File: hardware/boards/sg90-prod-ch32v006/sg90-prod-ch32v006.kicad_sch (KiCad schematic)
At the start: 36 parts, among them J1 Servo Input, J2 Motor, J3 Debug, J4 Potentiometer, Q1 AO3401A, U1 TPAP2210K-3.3TRG1, U2 SN74LVC2G07DRYR(UMW), U3 DRV8837DSGR-JSM, U4 CH32V006F8U6

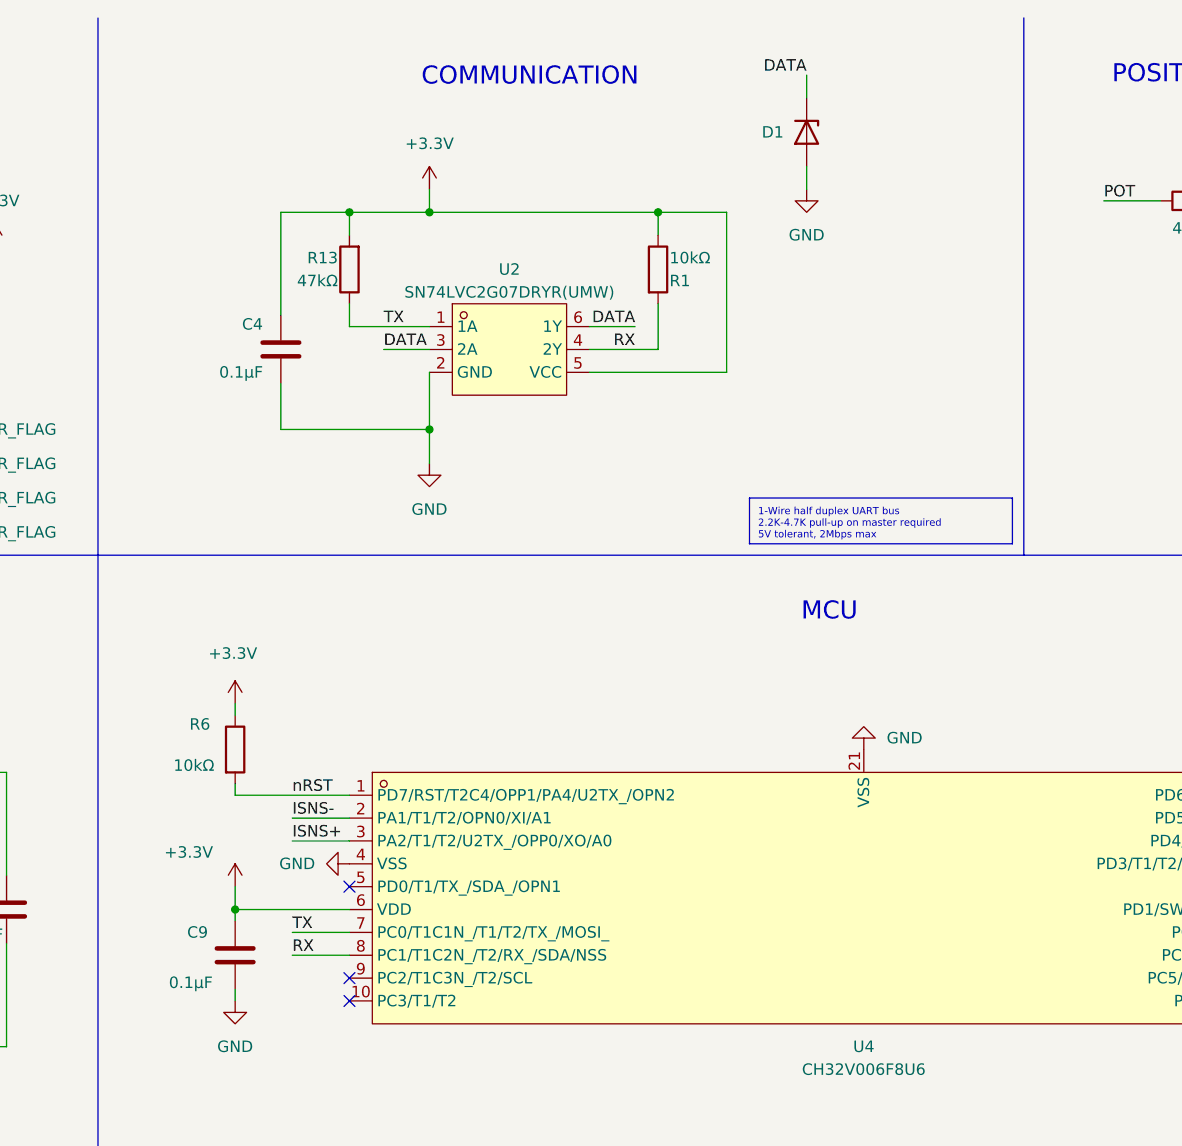
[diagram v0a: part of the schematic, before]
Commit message: Add X2-DFN1210-8 footprint and update schematics
- Add X2-DFN1210-8 footprint (1.2x1.0mm, 8-pin DFN)
- Add 3D models (STEP and WRL)
- Update shared symbol library
- Update sg90-prod-ch32v006 schematic
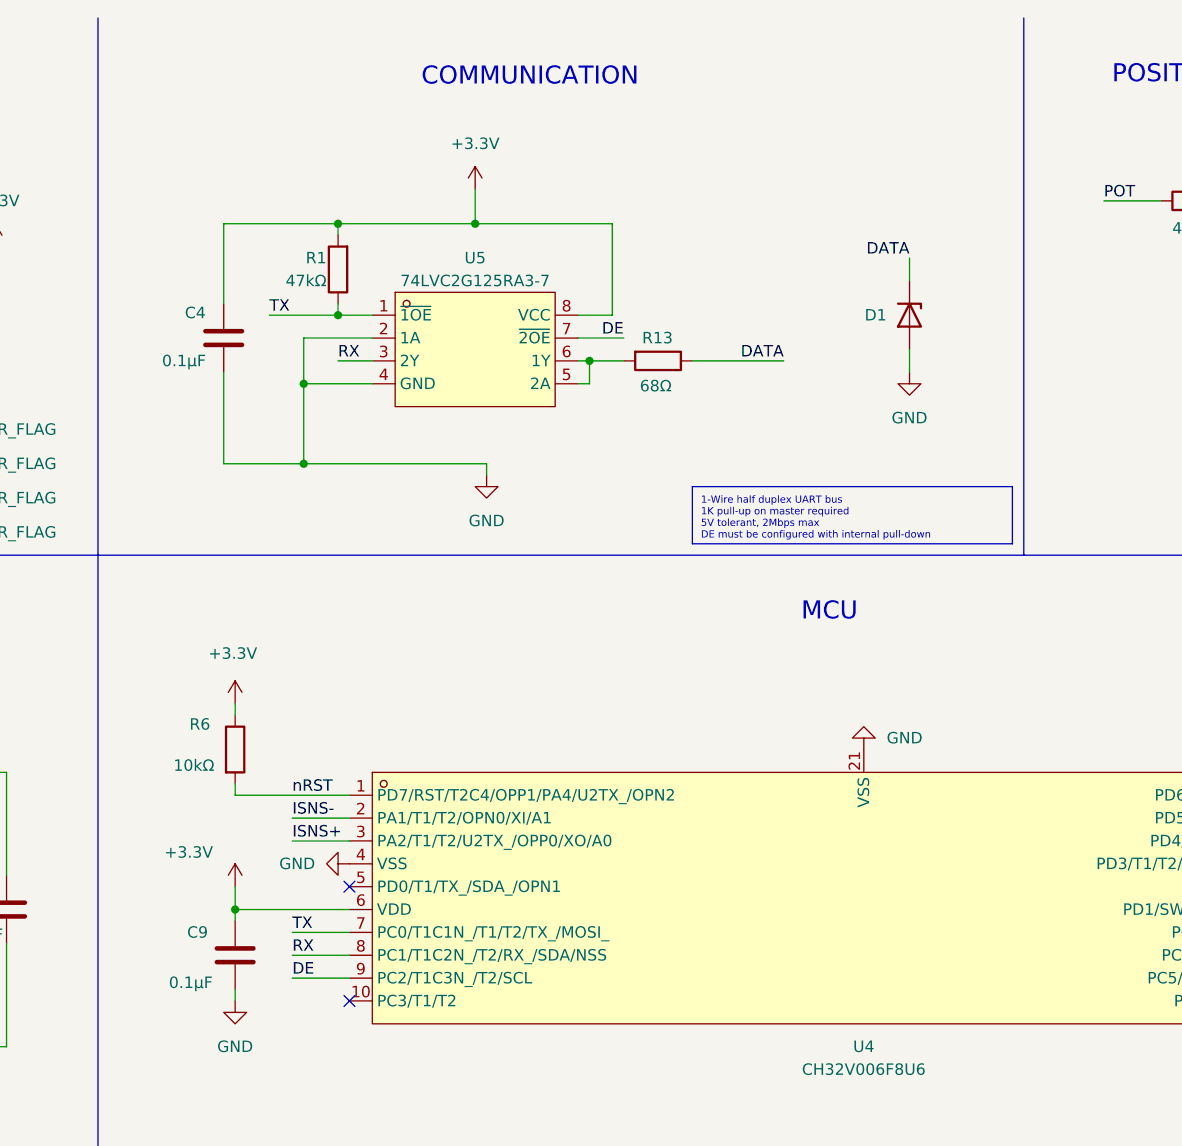
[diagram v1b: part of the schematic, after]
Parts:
- removed U2: SN74LVC2G07DRYR(UMW), shared:SON-6_L1.5-W1.0-P0.50-BL, symbol shared:SN74LVC2G07DRYR(UMW)
- added U5: 74LVC2G125RA3-7, shared:X2-DFN1210-8_L1.2-W1.0-P0.30-BL, symbol shared:74LVC2G125RA3-7
- R1: value 10kΩ -> 47kΩ; LCSC C11702 -> C25792
- R13: value 47kΩ -> 68Ω
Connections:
- net +3.3V: now also R1.2, U5.8 (VCC); no longer R1.1, R13.2
- net DATA: now also R13.1
- net GND: now also U5.2 (1A), U5.4 (GND)
- net RX: now also U5.3 (2Y); no longer R1.2
- net TX: now also R1.1, U5.1 (~{1OE}); no longer R13.1
- net DE: now reaches U4.9 (PC2/T1C3N_/T2/SCL)
- net DE: now also U5.7 (~{2OE})
- new net: R13.2, U5.5 (2A), U5.6 (1Y)
- no-connect marks 3 -> 2
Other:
- moved on the sheet: C4, D1

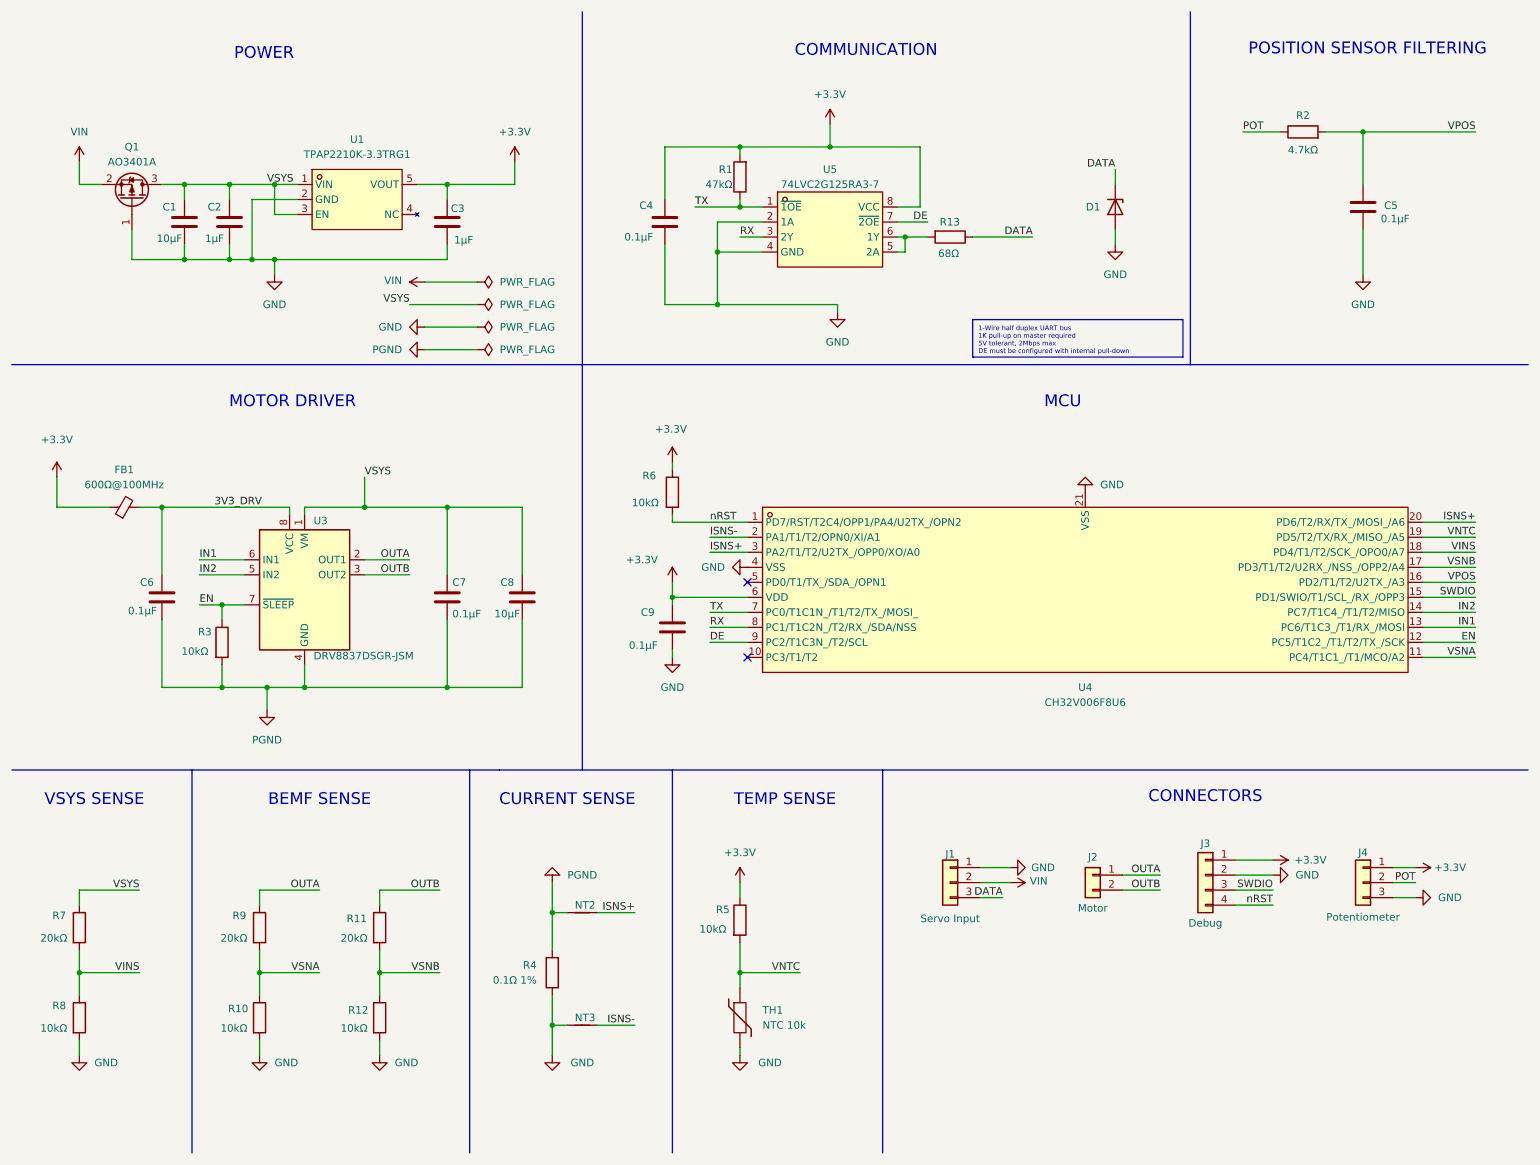
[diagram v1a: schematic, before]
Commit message: echo-free data line with RX disable latch
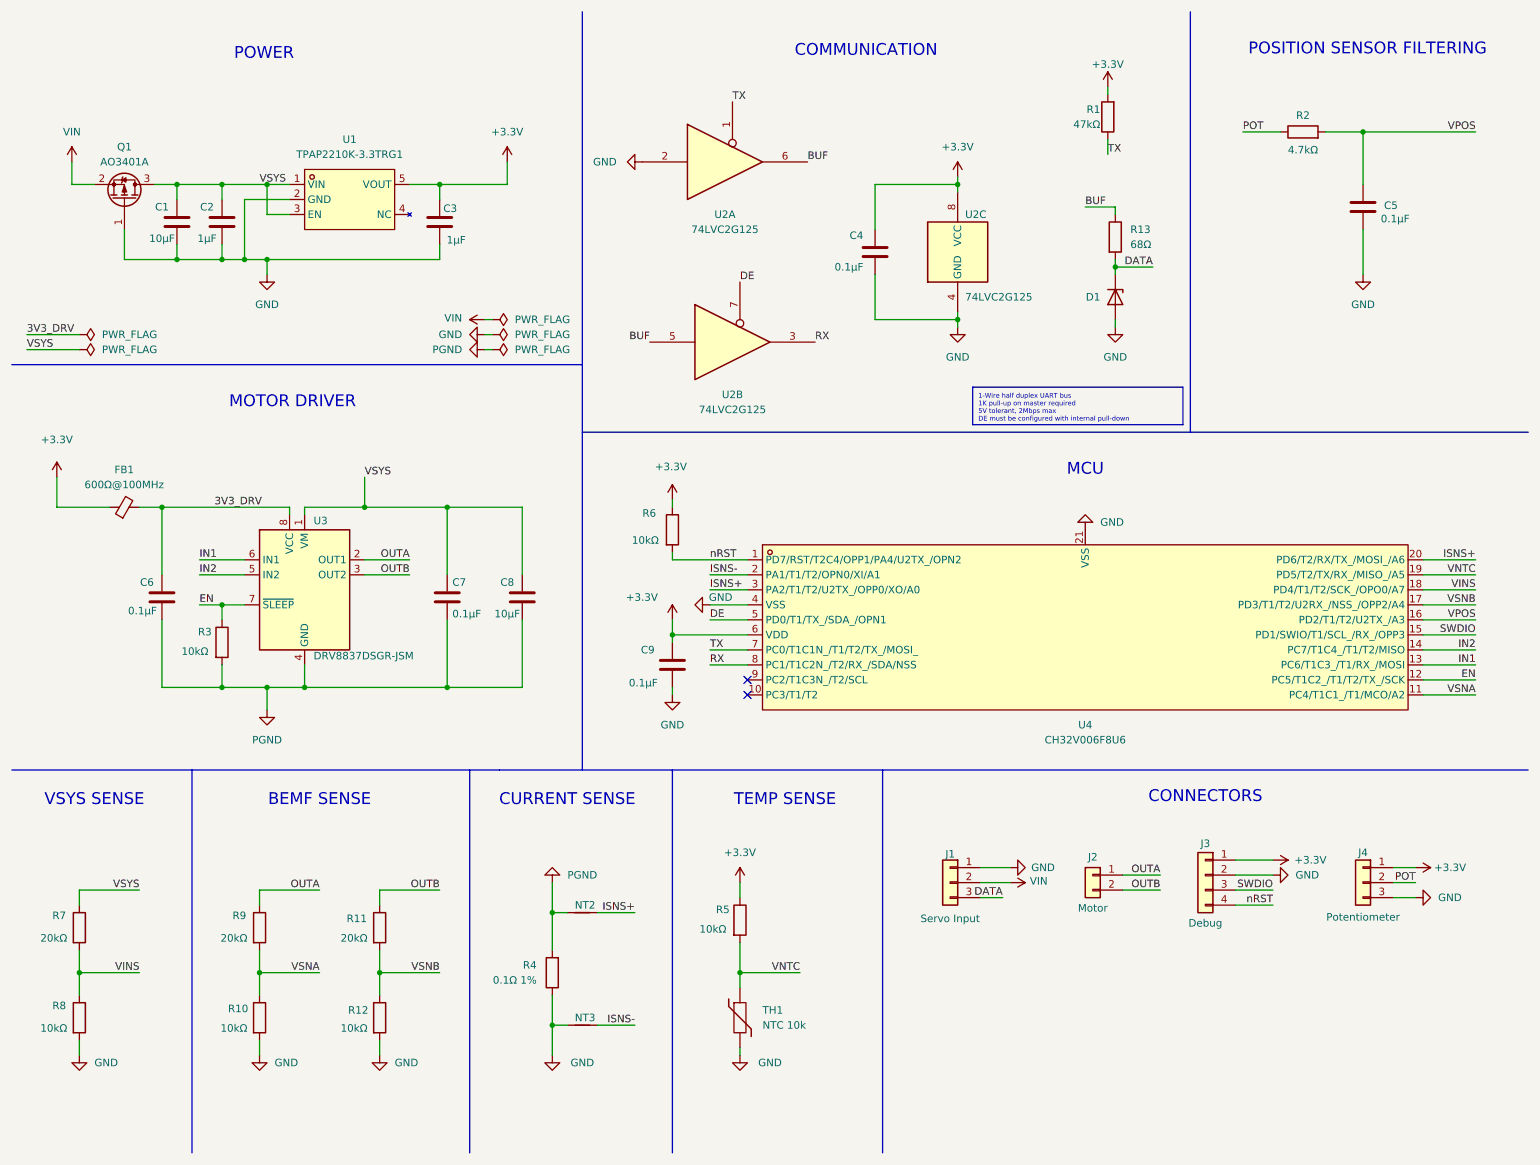
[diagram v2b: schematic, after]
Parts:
- removed U5: 74LVC2G125RA3-7, shared:X2-DFN1210-8_L1.2-W1.0-P0.30-BL, symbol shared:74LVC2G125RA3-7
- added U2: 74LVC2G125, shared:X2-DFN1210-8_L1.2-W1.0-P0.30-BL, symbol 74xGxx:74LVC2G125
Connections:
- net +3.3V: now also U2.8 (VCC)
- net DATA: now also R13.2; no longer R13.1
- net DE: now also U4.5 (PD0/T1/TX_/SDA_/OPN1), U2.7; no longer U4.9 (PC2/T1C3N_/T2/SCL)
- net GND: now also U2.2, U2.4 (GND)
- net RX: now also U2.3
- net TX: now also U2.1
- new net BUF: R13.1, U2.5, U2.6
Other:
- moved on the sheet: C1, C2, C3, C9, D1, Q1, R13, R6, U1, U4

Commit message: Normalize line endings to LF
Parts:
- removed NT3: NetTie_2, shared:NetTie-2_SMD_0.2mm, symbol Device:NetTie_2
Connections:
- net ISNS+ renamed ISNS
- net ISNS-: no longer names the net of U4.2 (PA1/T1/T2/OPN0/XI/A1)
- no-connect marks 2 -> 3
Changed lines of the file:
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@@
 	)
 	(junction
-		(at 102.87 182.88)
-		(diameter 0)
-		(color 0 0 0 0)
-	)
-	(junction
 		(at 73.66 173.99)
 		(diameter 0)
@@
 		(at 135.89 127)
 	)
+	(no_connect
+		(at 135.89 106.68)
+	)
 	(wire
 		(pts
@@
 	(wire
 		(pts
-			(xy 116.84 182.88) (xy 110.49 182.88)
-		)
-		(stroke
-			(width 0)
-			(type default)
-		)
-	)
-	(wire
-		(pts
 			(xy 91.44 63.5) (xy 92.71 63.5)
 		)
@@
 	(wire
 		(pts
-			(xy 102.87 182.88) (xy 102.87 187.96)
+			(xy 102.87 177.8) (xy 102.87 187.96)
 		)
 		(stroke
@@
 	(wire
 		(pts
-			(xy 105.41 182.88) (xy 102.87 182.88)
-		)
-		(stroke
-			(width 0)
-			(type default)
-		)
-	)
-	(wire
-		(pts
 			(xy 30.48 48.26) (xy 30.48 53.34)
 		)
@@
 	(wire
 		(pts
-			(xy 129.54 106.68) (xy 135.89 106.68)
-		)
-		(stroke
-			(width 0)
-			(type default)
-		)
-	)
-	(wire
-		(pts
 			(xy 196.85 24.13) (xy 196.85 25.4)
 		)
@@
 	(wire
 		(pts
-			(xy 102.87 177.8) (xy 102.87 182.88)
-		)
-		(stroke
-			(width 0)
-			(type default)
-		)
-	)
-	(wire
-		(pts
 			(xy 180.34 156.21) (xy 175.26 156.21)
 		)
@@
 		)
 	)
-	(label "ISNS+"
+	(label "ISNS"
 		(at 259.08 104.14 180)
 		(effects
@@
 		)
 	)
-	(label "ISNS-"
-		(at 129.54 106.68 0)
-		(effects
-			(font
-				(size 1.27 1.27)
-			)
-			(justify left bottom)
-		)
-	)
 	(label "TX"
 		(at 196.85 35.56 0)
@@
 		)
 	)
-	(label "ISNS+"
+	(label "ISNS"
 		(at 129.54 109.22 0)
 		(effects
@@
 		)
 	)
-	(label "ISNS+"
+	(label "ISNS"
 		(at 116.84 163.83 180)
 		(effects
@@
 		)
 	)
-	(label "ISNS-"
-		(at 116.84 182.88 180)
-		(effects
-			(font
-				(size 1.27 1.27)
-			)
-			(justify right bottom)
-		)
-	)
 	(label "DATA"
 		(at 204.47 54.61 180)
@@
 					(unit 1)
 				)
-			)
-		)
-	)
-	(symbol
-		(lib_id "Device:NetTie_2")
-		(at 107.95 182.88 180)
-		(unit 1)
-		(exclude_from_sim no)
-		(in_bom no)
-		(on_board yes)
-		(dnp no)
-		(property "Reference" "NT3"
-			(at 106.68 181.61 0)
-			(effects
-				(font
-					(size 1.27 1.27)
-				)
-				(justify right)
-			)
-		)
-		(property "Value" "NetTie_2"
-			(at 109.2199 181.61 90)
-			(effects
-				(font
-					(size 1.27 1.27)
-				)
-				(justify right)
-				(hide yes)
-			)
-		)
-		(property "Footprint" "shared:NetTie-2_SMD_0.2mm"
-			(at 107.95 182.88 0)
-			(effects
-				(font
-					(size 1.27 1.27)
-				)
-				(hide yes)
-			)
-		)
-		(property "Datasheet" "~"
-			(at 107.95 182.88 0)
-			(effects
-				(font
-					(size 1.27 1.27)
-				)
-				(hide yes)
-			)
-		)
-		(property "Description" "Net tie, 2 pins"
-			(at 107.95 182.88 0)
-			(effects
-				(font
-					(size 1.27 1.27)
-				)
-				(hide yes)
-			)
-		)
-		(pin "2"
-		)
-		(pin "1"
-		)
-		(instances
-			(project "sg90-prod-ch32v006"
-				(path "/6062e7d2-0c72-467e-b49c-6387ba053e09"
-					(reference "NT3")
-					(unit 1)
-				)

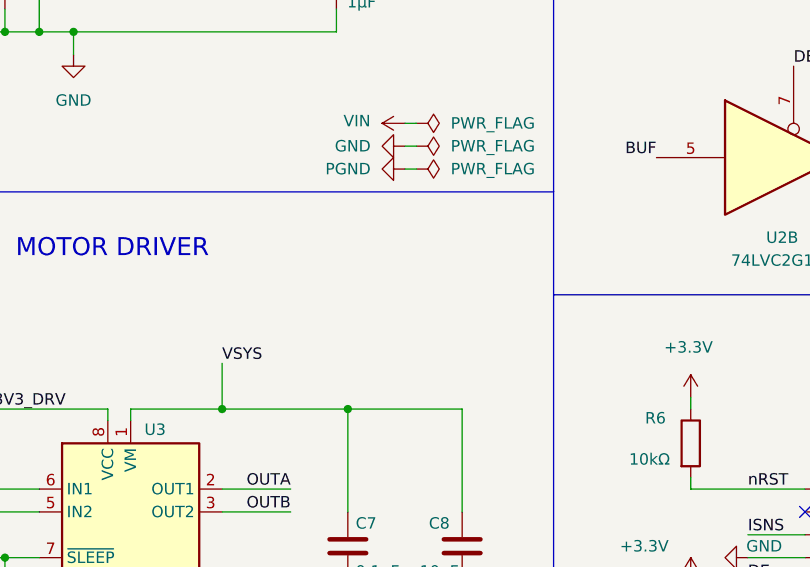
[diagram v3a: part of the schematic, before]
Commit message: add 0.1uF cap between motor terminals to reduce EMI
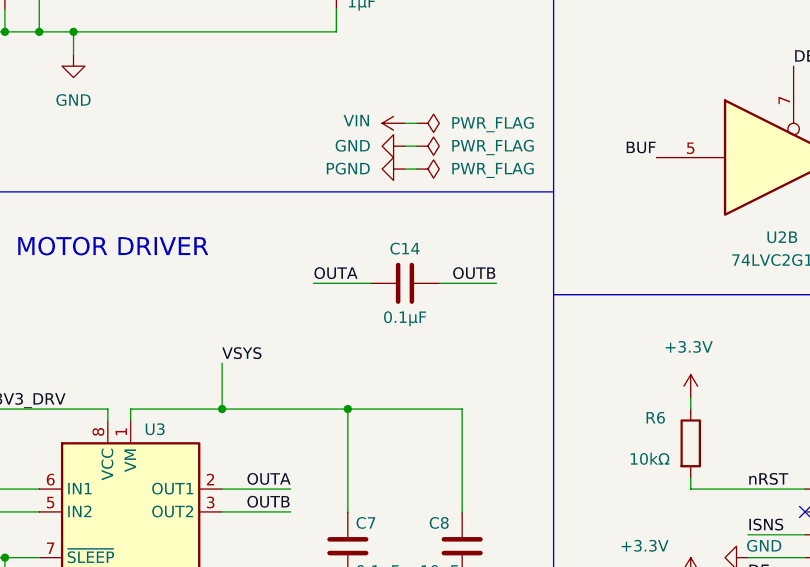
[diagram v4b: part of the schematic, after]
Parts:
- added C14: 0.1µF, Capacitor_SMD:C_0402_1005Metric, symbol Device:C
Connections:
- net OUTA: now also C14.1
- net OUTB: now also C14.2
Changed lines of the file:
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@@
 		)
 	)
+	(wire
+		(pts
+			(xy 81.28 81.28) (xy 87.63 81.28)
+		)
+		(stroke
+			(width 0)
+			(type default)
+		)
+	)
 	(polyline
 		(pts
@@
 	(wire
 		(pts
+			(xy 95.25 81.28) (xy 101.6 81.28)
+		)
+		(stroke
+			(width 0)
+			(type default)
+		)
+	)
+	(wire
+		(pts
 			(xy 30.48 48.26) (xy 30.48 53.34)
 		)
@@
 		)
 	)
+	(label "OUTB"
+		(at 101.6 81.28 180)
+		(effects
+			(font
+				(size 1.27 1.27)
+			)
+			(justify right bottom)
+		)
+	)
 	(label "VPOS"
 		(at 259.08 114.3 180)
@@
 		)
 	)
+	(label "OUTA"
+		(at 81.28 81.28 0)
+		(effects
+			(font
+				(size 1.27 1.27)
+			)
+			(justify left bottom)
+		)
+	)
 	(label "VINS"
 		(at 33.02 173.99 180)
@@
 					(unit 1)
 				)
+			)
+		)
+	)
+	(symbol
+		(lib_id "Device:C")
+		(at 91.44 81.28 90)
+		(unit 1)
+		(exclude_from_sim no)
+		(in_bom yes)
+		(on_board yes)
+		(dnp no)
+		(property "Reference" "C14"
+			(at 91.44 77.47 90)
+			(effects
+				(font
+					(size 1.27 1.27)
+				)
+			)
+		)
+		(property "Value" "0.1µF"
+			(at 91.44 85.09 90)
+			(effects
+				(font
+					(size 1.27 1.27)
+				)
+			)
+		)
+		(property "Footprint" "Capacitor_SMD:C_0402_1005Metric"
+			(at 71.13 118.9548 0)
+			(effects
+				(font
+					(size 1.27 1.27)
+				)
+				(hide yes)
+			)
+		)
+		(property "Datasheet" "~"
+			(at 67.32 119.92 0)
+			(effects
+				(font
+					(size 1.27 1.27)
+				)
+				(hide yes)
+			)
+		)
+		(property "Description" "Unpolarized capacitor"
+			(at 67.32 119.92 0)
+			(effects
+				(font
+					(size 1.27 1.27)
+				)
+				(hide yes)
+			)
+		)
+		(property "LCSC" "C1525"
+			(at 88.9 79.248 0)
+			(effects
+				(font
+					(size 1.27 1.27)
+				)
+				(hide yes)
+			)
+		)
+		(pin "1"
+		)
+		(pin "2"
+		)
+		(instances
+			(project "sg90-prod-ch32v006"
+				(path "/6062e7d2-0c72-467e-b49c-6387ba053e09"
+					(reference "C14")
+					(unit 1)
+				)
